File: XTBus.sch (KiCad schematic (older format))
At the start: 33 parts, among them IC1 74LS157, IC10 74LS138, IC11 74LS138, IC12 74LS139, IC13 74LS245, IC14 D7201C, IC15 D8253C-5, IC2 74LS09, IC3 SN75176AP, IC4 SN75176AP, IC5 74LS123, IC6 74LS393, IC7 74LS14, IC8 74LS04, IC9 74LS11, J1 DB9_Female, J2 Bus_ISA_8bit

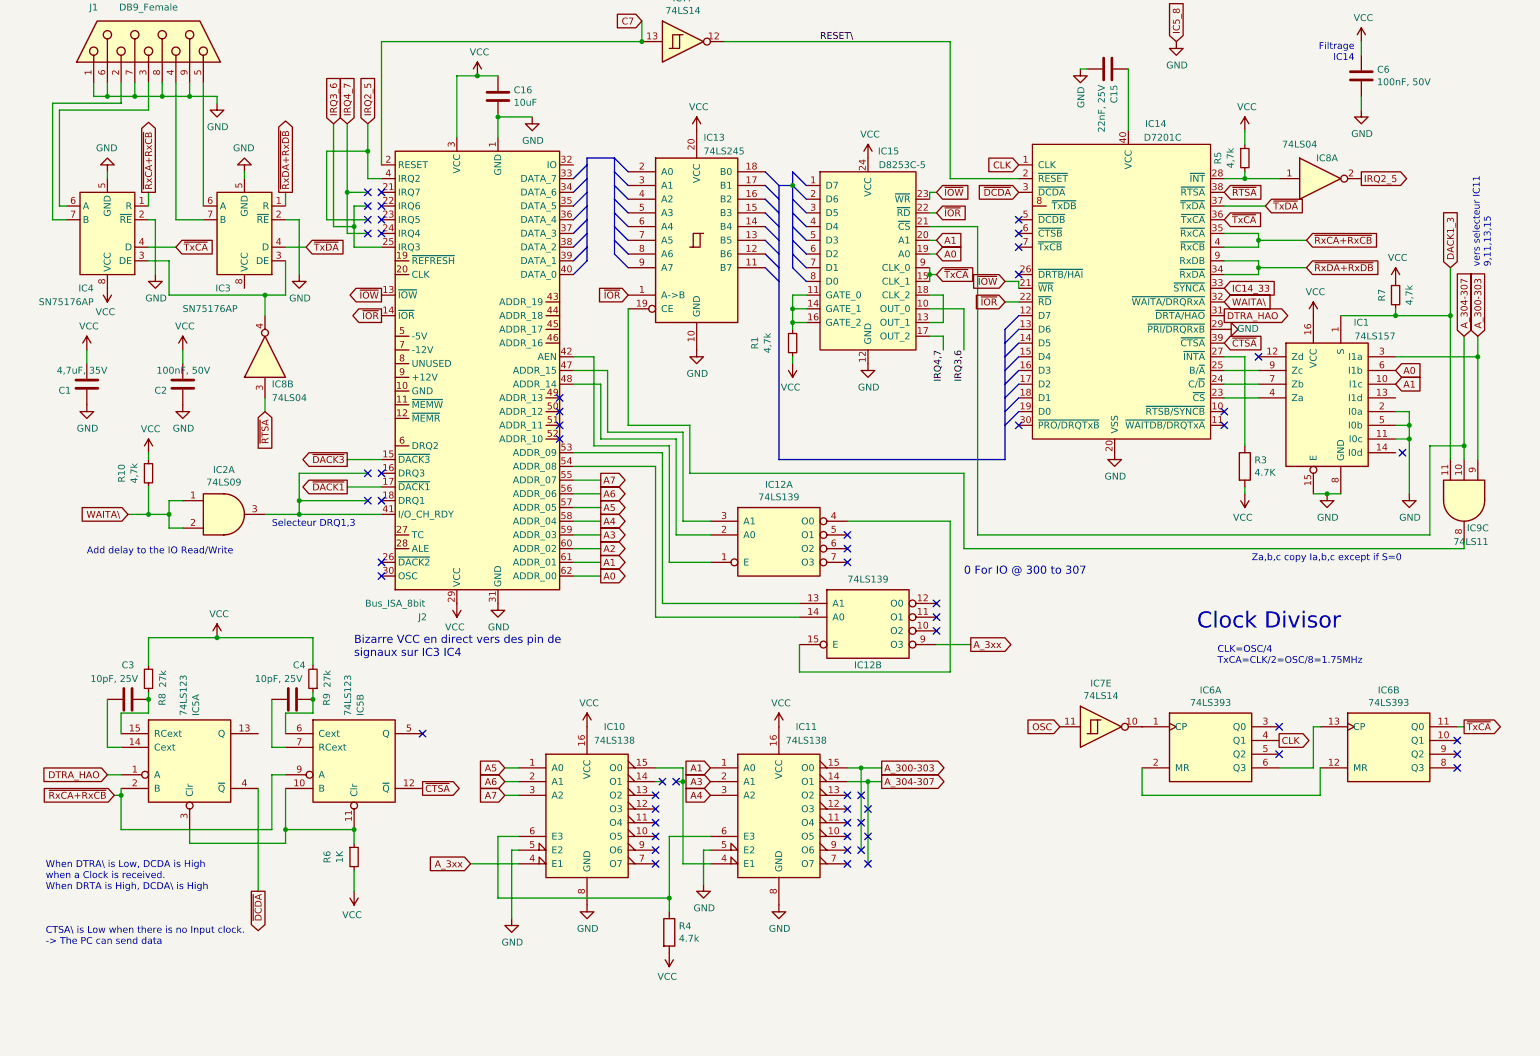
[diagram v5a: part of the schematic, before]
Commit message: Dernière version avec les valeurs actuelles de capa et résistance.
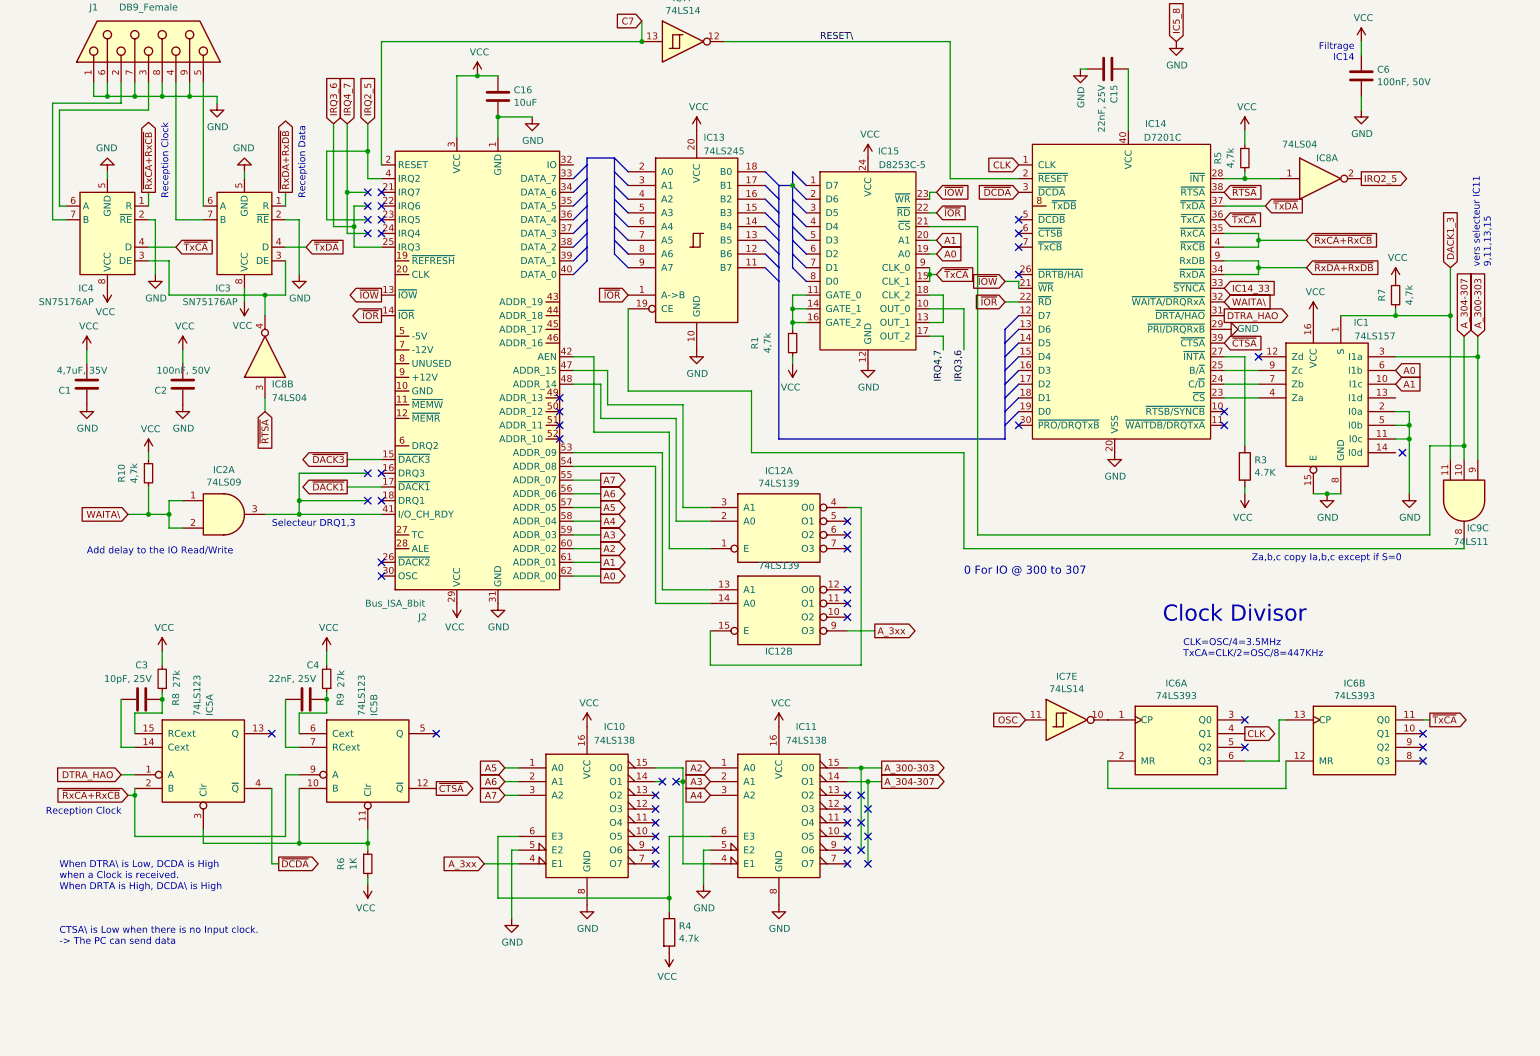
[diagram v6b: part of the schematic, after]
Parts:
- C4: value 10pF, 25V -> 22nF, 25V
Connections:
- net A1: no longer IC11.1 (A0)
- net A2: now also IC11.1 (A0)
- net VCC: now also IC3.8 (VCC)
- no-connect marks 59 -> 60
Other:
- note added: "CLK=OSC/4=3.5MHz\nTxCA=CLK/2=OSC/8=447KHz"
- note added: "Reception Clock"
- note added: "Reception Data"
- note removed: "Bizarre VCC en direct vers des pin de \nsignaux sur IC3 IC4"
- note removed: "CLK=OSC/4\nTxCA=CLK/2=OSC/8=1.75MHz"
- moved on the sheet: C3, C4, IC12A, IC12B, IC5A, IC5B, IC6A, IC6B, IC7E, R6, R8, R9

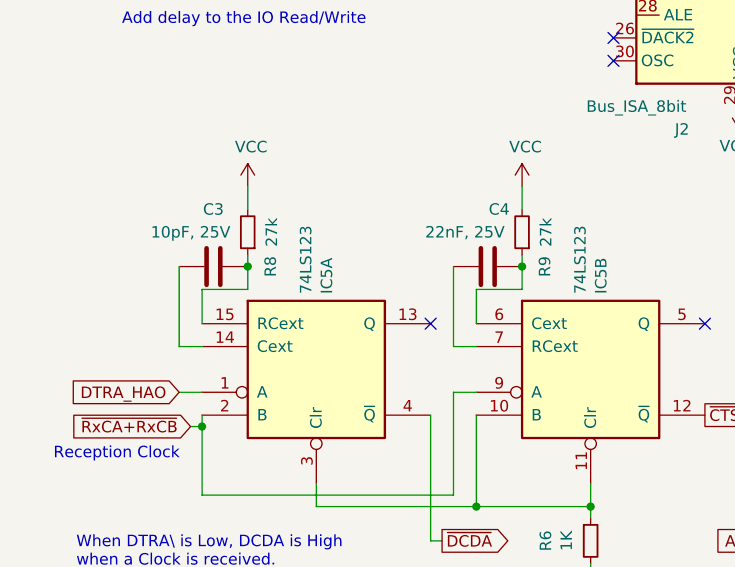
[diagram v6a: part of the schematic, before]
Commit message: Corrrection BOM et petite correction Schéma
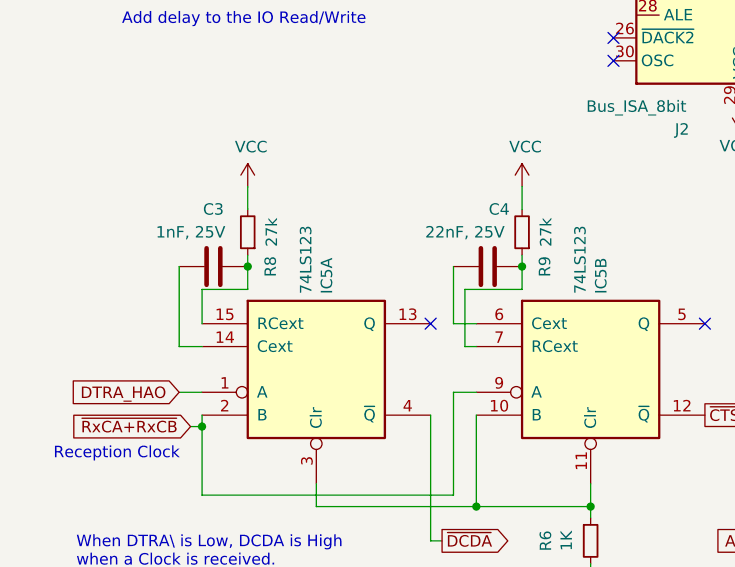
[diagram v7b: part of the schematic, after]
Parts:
- C3: value 10pF, 25V -> 1nF, 25V
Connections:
- net at C4.2, R9.1: now also IC5.7 (RCext); no longer IC5.6 (Cext)
- net at C4.1: now also IC5.6 (Cext); no longer IC5.7 (RCext)
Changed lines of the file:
@@
 AR Path="/6126F7E9/61CC5FA2" Ref="C3"  Part="1"
 F 0 "C3" V 1500 5700 50  0000 C CNN
-F 1 "10pF, 25V" V 1400 5800 50  0000 C CNN
+F 1 "1nF, 25V" V 1400 5800 50  0000 C CNN
 F 2 "Capacitor_THT:C_Disc_D5.0mm_W2.5mm_P5.00mm" H 1288 5550 50  0001 C CNN
 F 3 "~" H 1250 5700 50  0001 C CNN
@@
 $EndComp
 Wire Wire Line
-	2400 5950 2400 5800
-Wire Wire Line
-	2400 5800 2600 5800
-Wire Wire Line
-	2600 5800 2600 5700
-Wire Wire Line
 	1400 5800 1200 5800
 Wire Wire Line
@@
 Wire Wire Line
 	1100 6050 1200 6050
-Connection ~ 2600 5700
 Wire Wire Line
 	2600 5700 2600 5650
-Wire Wire Line
-	2300 5700 2300 6050
-Wire Wire Line
-	2300 6050 2400 6050
 Wire Wire Line
 	1200 6350 1200 6400
@@
 Entry Bus Bus
 	6000 2050 6100 2150
+Wire Wire Line
+	2400 5950 2300 5950
+Wire Wire Line
+	2300 5950 2300 5700
+Wire Wire Line
+	2400 6050 2350 6050
+Wire Wire Line
+	2350 6050 2350 5800
+Wire Wire Line
+	2350 5800 2600 5800
+Wire Wire Line
+	2600 5800 2600 5700
 Wire Bus Line
 	6000 1950 6000 2550
@@
 Wire Bus Line
 	7550 3000 7550 3800
+Connection ~ 2600 5700
 $EndSCHEMATC

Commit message: Maj de Freddy
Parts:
- added R2: 4.7K, symbol Device:R
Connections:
- net VCC: now also R2.1
- net at IC5.6 (Cext): now also C4.2, R9.1; no longer C4.1
- net IC14_33: no longer names the net of IC14.33 (~SYNCA)
- net IC14_33: now also R2.2
- new net: C4.1, IC5.7 (RCext)
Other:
- note added: "200us Delay : Silence Detection"
- note added: "5us Delay : Clock Detection"
- note added: "When DTRA\ is Low: DCDA is Low\nwhen a Clock is received.\nWhen DTRA\ is High, DCDA\ is High"
- note removed: "When DTRA\ is Low, DCDA is High\nwhen a Clock is received.\nWhen DRTA is High, DCDA\ is High"
- moved on the sheet: R7
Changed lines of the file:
@@
 L Device:R_Small R?
 U 1 1 61633523
-P 10400 2750
+P 10600 2700
 AR Path="/61633523" Ref="R?"  Part="1"
 AR Path="/6123EC51/61633523" Ref="R?"  Part="1"
 AR Path="/6126F7E9/61633523" Ref="R7"  Part="1"
-F 0 "R7" V 10300 2750 50  0000 C CNN
-F 1 "4,7k" V 10500 2750 50  0000 C CNN
-F 2 "Resistor_THT:R_Axial_DIN0309_L9.0mm_D3.2mm_P12.70mm_Horizontal" H 10400 2750 50  0001 C CNN
-F 3 "~" H 10400 2750 50  0001 C CNN
-	1    10400 2750
+F 0 "R7" V 10500 2700 50  0000 C CNN
+F 1 "4,7k" V 10700 2700 50  0000 C CNN
+F 2 "Resistor_THT:R_Axial_DIN0309_L9.0mm_D3.2mm_P12.70mm_Horizontal" H 10600 2700 50  0001 C CNN
+F 3 "~" H 10600 2700 50  0001 C CNN
+	1    10600 2700
 	1    0    0    -1
 $EndComp
@@
 	11000 3200 11000 3950
 Wire Wire Line
-	10000 2900 10400 2900
-Wire Wire Line
 	10500 3600 10500 3700
 Wire Wire Line
@@
 $EndComp
 Wire Wire Line
+	2400 5950 2400 5800
+Wire Wire Line
+	2400 5800 2600 5800
+Wire Wire Line
+	2600 5800 2600 5700
+Wire Wire Line
 	1400 5800 1200 5800
 Wire Wire Line
@@
 Wire Wire Line
 	1100 6050 1200 6050
+Connection ~ 2600 5700
 Wire Wire Line
 	2600 5700 2600 5650
+Wire Wire Line
+	2300 5700 2300 6050
+Wire Wire Line
+	2300 6050 2400 6050
 Wire Wire Line
 	1200 6350 1200 6400
@@
 Text GLabel 1150 6400 0    50   Input ~ 0
 ~RxCA+RxCB
-Text GLabel 9150 2700 2    50   Input ~ 0
-IC14_33
-Wire Wire Line
-	10400 2900 10400 2850
 Text GLabel 7050 2600 2    50   Input ~ 0
 ~TxCA
@@
 L power:VCC #PWR?
 U 1 1 61E9B4AD
-P 9800 2900
-F 0 "#PWR?" H 9800 2750 50  0001 C CNN
-F 1 "VCC" H 9815 3073 50  0000 C CNN
-F 2 "" H 9800 2900 50  0001 C CNN
-F 3 "" H 9800 2900 50  0001 C CNN
-	1    9800 2900
-	1    0    0    -1
-$EndComp
-Wire Wire Line
-	10400 2900 10800 2900
-Wire Wire Line
-	10800 2900 10800 3950
-Connection ~ 10400 2900
-Wire Wire Line
-	10800 2900 10800 2550
-Connection ~ 10800 2900
+P 9900 2700
+F 0 "#PWR?" H 9900 2550 50  0001 C CNN
+F 1 "VCC" H 9915 2873 50  0000 C CNN
+F 2 "" H 9900 2700 50  0001 C CNN
+F 3 "" H 9900 2700 50  0001 C CNN
+	1    9900 2700
+	0    1    1    0
+$EndComp
 $Comp
 L power:VCC #PWR?
 U 1 1 61F0E658
-P 10400 2650
-F 0 "#PWR?" H 10400 2500 50  0001 C CNN
-F 1 "VCC" H 10415 2823 50  0000 C CNN
-F 2 "" H 10400 2650 50  0001 C CNN
-F 3 "" H 10400 2650 50  0001 C CNN
-	1    10400 2650
+P 10600 2600
+F 0 "#PWR?" H 10600 2450 50  0001 C CNN
+F 1 "VCC" H 10615 2773 50  0000 C CNN
+F 2 "" H 10600 2600 50  0001 C CNN
+F 3 "" H 10600 2600 50  0001 C CNN
+	1    10600 2600
 	1    0    0    -1
 $EndComp
@@
 NoConn ~ 5050 6300
 Text Notes 650  7100 0    50   ~ 0
-When DTRA\ is Low, DCDA is High\nwhen a Clock is received.\nWhen DRTA is High, DCDA\ is High
+When DTRA\ is Low: DCDA is Low\nwhen a Clock is received.\nWhen DTRA\ is High, DCDA\ is High
 Text Notes 650  7500 0    50   ~ 0
 CTSA\ is Low when there is no Input clock.\n-> The PC can send data
 Text Notes 8850 5400 0    50   ~ 0
 CLK=OSC/4=3.5MHz\nTxCA=CLK/2=OSC/8=447KHz
-Text GLabel 10800 2550 1    50   Input ~ 0
+Text GLabel 10800 2750 1    50   Input ~ 0
 DACK1_3
 NoConn ~ 3000 4700
@@
 Entry Bus Bus
 	6000 2050 6100 2150
-Wire Wire Line
-	2400 5950 2300 5950
-Wire Wire Line
-	2300 5950 2300 5700
-Wire Wire Line
-	2400 6050 2350 6050
-Wire Wire Line
-	2350 6050 2350 5800
-Wire Wire Line
-	2350 5800 2600 5800
-Wire Wire Line
-	2600 5800 2600 5700
+Text Notes 500  5100 0    50   ~ 0
+5us Delay : Clock Detection
+Text Notes 2750 5400 0    50   ~ 0
+200us Delay : Silence Detection
+Entry Wire Line
+	-10350 7850 -10250 7950
+Entry Wire Line
+	-10350 7850 -10250 7950
+Entry Wire Line
+	-10350 7850 -10250 7950
+Entry Wire Line
+	-10350 7850 -10250 7950
+Entry Wire Line
+	-10350 7850 -10250 7950
+Entry Wire Line
+	-10350 7850 -10250 7950
+Entry Wire Line
+	-10350 7850 -10250 7950
+Entry Wire Line
+	-10350 7850 -10250 7950
+Entry Wire Line
+	-2800 7750 -2700 7850
+Entry Wire Line
+	-5200 7800 -5100 7900
+Entry Wire Line
+	-3900 7750 -3800 7850
+Entry Wire Line
+	3650 4400 3750 4500
+Entry Wire Line
+	3600 4400 3700 4500
+Entry Wire Line
+	3650 4350 3750 4450
+Wire Wire Line
+	10800 2900 10800 2750
+Wire Wire Line
+	10800 2900 10800 3950
+Connection ~ 10800 2900
+Wire Wire Line
+	10000 2900 10600 2900
+Wire Wire Line
+	10600 2800 10600 2900
+Connection ~ 10600 2900
+Wire Wire Line
+	10600 2900 10800 2900
+$Comp
+L Device:R R2
+U 1 1 61F0AA5F
+P 9600 2700
+F 0 "R2" V 9500 2650 50  0000 L CNN
+F 1 "4.7K" V 9700 2650 50  0000 L CNN
+F 2 "" V 9530 2700 50  0001 C CNN
+F 3 "~" H 9600 2700 50  0001 C CNN
+	1    9600 2700
+	0    1    1    0
+$EndComp
+Wire Wire Line
+	9150 2700 9450 2700
+Wire Wire Line
+	9750 2700 9800 2700
+Wire Wire Line
+	9800 2900 9800 2700
+Connection ~ 9800 2700
+Wire Wire Line
+	9800 2700 9900 2700
 Wire Bus Line
 	6000 1950 6000 2550
@@
 Wire Bus Line
 	7550 3000 7550 3800
-Connection ~ 2600 5700
 $EndSCHEMATC
